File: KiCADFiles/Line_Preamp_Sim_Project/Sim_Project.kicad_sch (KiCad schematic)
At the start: 26 parts, among them U1 OPA1655D, U6 OPA1655D

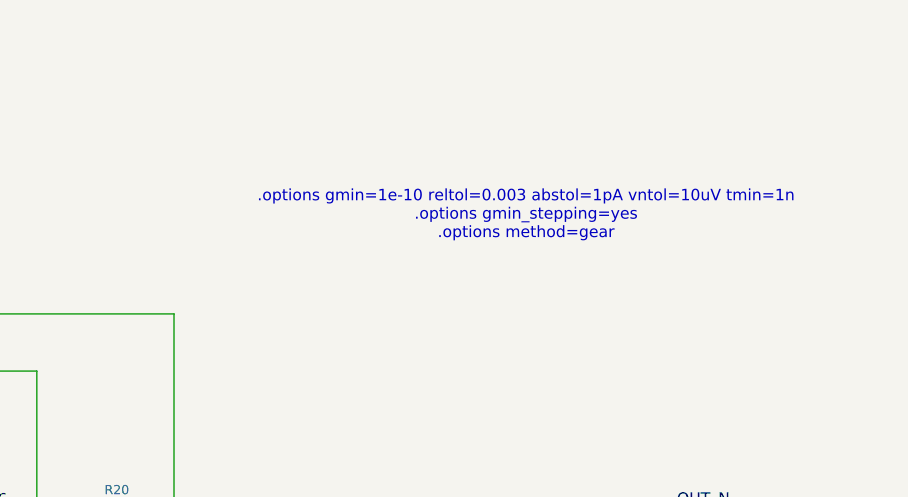
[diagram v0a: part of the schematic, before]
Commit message: removed connectors and condensed layout
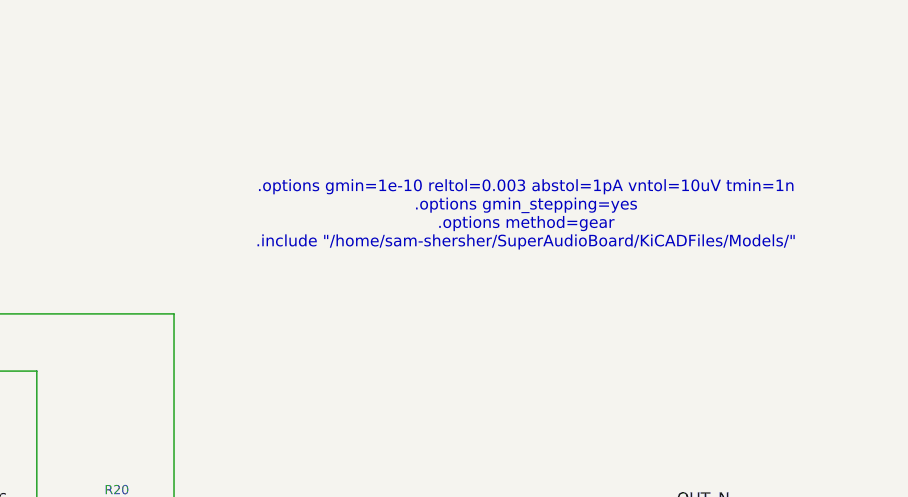
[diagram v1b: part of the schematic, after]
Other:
- note added: ".options gmin=1e-10 reltol=0.003 abstol=1pA vntol=10uV tmin=1n .options gmin_stepping=yes .options method=gear .include "/home/sam-shersher/SuperAudioBoard/KiCADFiles/Models/""
- note removed: ".options gmin=1e-10 reltol=0.003 abstol=1pA vntol=10uV tmin=1n .options gmin_stepping=yes .options method=gear"
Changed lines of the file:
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@@
 	(generator_version "9.0")
 	(paper "A4")
-	(text ".options gmin=1e-10 reltol=0.003 abstol=1pA vntol=10uV tmin=1n\n.options gmin_stepping=yes\n.options method=gear"
+	(text ".options gmin=1e-10 reltol=0.003 abstol=1pA vntol=10uV tmin=1n\n.options gmin_stepping=yes\n.options method=gear\n.include \"/home/sam-shersher/SuperAudioBoard/KiCADFiles/Models/\""
 		(exclude_from_sim no)
 		(at 204.216 51.308 0)
